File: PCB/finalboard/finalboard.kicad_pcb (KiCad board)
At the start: 2 copper layers, 132.1 x 76.2 mm, 1 part, among them U1 ESP32-S3-WROOM-1

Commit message: FinalBoard Changes
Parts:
- added U3: USBLC6-2SC6, Package_TO_SOT_SMD:SOT-23-6, F.Cu at (95.4, 93.0)
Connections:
- U1 pad 13: unconnected-(U1-GPIO19/U1RTS/ADC2_CH8/CLK_OUT2/USB_D--Pad13) -> /USB_D-
- U1 pad 14: unconnected-(U1-GPIO20/U1CTS/ADC2_CH9/CLK_OUT1/USB_D+-Pad14) -> /USB_D+
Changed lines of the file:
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@@
   (net 11 "unconnected-(U1-GPIO18{slash}U1RXD{slash}ADC2_CH7{slash}CLK_OUT3-Pad11)")
   (net 12 "unconnected-(U1-GPIO8{slash}TOUCH8{slash}ADC1_CH7{slash}SUBSPICS1-Pad12)")
-  (net 13 "unconnected-(U1-GPIO19{slash}U1RTS{slash}ADC2_CH8{slash}CLK_OUT2{slash}USB_D--Pad13)")
-  (net 14 "unconnected-(U1-GPIO20{slash}U1CTS{slash}ADC2_CH9{slash}CLK_OUT1{slash}USB_D+-Pad14)")
+  (net 13 "/USB_D-")
+  (net 14 "/USB_D+")
   (net 15 "unconnected-(U1-GPIO3{slash}TOUCH3{slash}ADC1_CH2-Pad15)")
   (net 16 "unconnected-(U1-GPIO46-Pad16)")
@@
   (net 38 "unconnected-(U1-GPIO2{slash}TOUCH2{slash}ADC1_CH1-Pad38)")
   (net 39 "unconnected-(U1-GPIO1{slash}TOUCH1{slash}ADC1_CH0-Pad39)")
+  (net 40 "/D+")
+  (net 41 "GND")
+  (net 42 "/D-")
+  (net 43 "Net-(J1-D--PadA7)")
+  (net 44 "Net-(U3-VBUS)")
+  (net 45 "Net-(J1-D+-PadA6)")
   (footprint "wc_sys_footprint:ESP32-S3-WROOM-1U" (layer "F.Cu")
     (at 95.39 60.33)
@@
       (net 12 "unconnected-(U1-GPIO8{slash}TOUCH8{slash}ADC1_CH7{slash}SUBSPICS1-Pad12)") (pinfunction "GPIO8/TOUCH8/ADC1_CH7/SUBSPICS1") (pintype "bidirectional"))
     (pad "13" smd rect (at -8.75 6.98) (size 1.5 0.9) (layers "F.Cu" "F.Paste" "F.Mask")
-      (net 13 "unconnected-(U1-GPIO19{slash}U1RTS{slash}ADC2_CH8{slash}CLK_OUT2{slash}USB_D--Pad13)") (pinfunction "GPIO19/U1RTS/ADC2_CH8/CLK_OUT2/USB_D-") (pintype "bidirectional"))
+      (net 13 "/USB_D-") (pinfunction "GPIO19/U1RTS/ADC2_CH8/CLK_OUT2/USB_D-") (pintype "bidirectional"))
     (pad "14" smd rect (at -8.75 8.25) (size 1.5 0.9) (layers "F.Cu" "F.Paste" "F.Mask")
-      (net 14 "unconnected-(U1-GPIO20{slash}U1CTS{slash}ADC2_CH9{slash}CLK_OUT1{slash}USB_D+-Pad14)") (pinfunction "GPIO20/U1CTS/ADC2_CH9/CLK_OUT1/USB_D+") (pintype "bidirectional"))
+      (net 14 "/USB_D+") (pinfunction "GPIO20/U1CTS/ADC2_CH9/CLK_OUT1/USB_D+") (pintype "bidirectional"))
     (pad "15" smd rect (at -6.985 9.5 90) (size 1.5 0.9) (layers "F.Cu" "F.Paste" "F.Mask")
       (net 15 "unconnected-(U1-GPIO3{slash}TOUCH3{slash}ADC1_CH2-Pad15)") (pinfunction "GPIO3/TOUCH3/ADC1_CH2") (pintype "bidirectional"))
@@
       (scale (xyz 1 1 1))
       (rotate (xyz 0 0 0))
+    )
+  )
+  (footprint "Package_TO_SOT_SMD:SOT-23-6" (layer "F.Cu")
+    (at 95.3825 93.03)
+    (descr "SOT, 6 Pin (https://www.jedec.org/sites/default/files/docs/Mo-178c.PDF variant AB), generated with kicad-footprint-generator ipc_gullwing_generator.py")
+    (tags "SOT TO_SOT_SMD")
+    (property "Sheetfile" "finalboard.kicad_sch")
+    (property "Sheetname" "")
+    (property "ki_description" "Very low capacitance ESD protection diode, 2 data-line, SOT-23-6")
+    (property "ki_keywords" "usb ethernet video")
+    (attr smd)
+    (fp_text reference "U3" (at 0 -2.4) (layer "F.SilkS")
+        (effects (font (size 1 1) (thickness 0.15)))
+    )
+    (fp_text value "USBLC6-2SC6" (at 0 2.4) (layer "F.Fab")
+        (effects (font (size 1 1) (thickness 0.15)))
+    )
+    (fp_text user "${REFERENCE}" (at 0 0) (layer "F.Fab")
+        (effects (font (size 0.4 0.4) (thickness 0.06)))
+    )
+    (fp_line (start 0 -1.56) (end -1.8 -1.56)
+      (stroke (width 0.12) (type solid)) (layer "F.SilkS"))
+    (fp_line (start 0 -1.56) (end 0.8 -1.56)
+      (stroke (width 0.12) (type solid)) (layer "F.SilkS"))
+    (fp_line (start 0 1.56) (end -0.8 1.56)
+      (stroke (width 0.12) (type solid)) (layer "F.SilkS"))
+    (fp_line (start 0 1.56) (end 0.8 1.56)
+      (stroke (width 0.12) (type solid)) (layer "F.SilkS"))
+    (fp_line (start -2.05 -1.7) (end -2.05 1.7)
+      (stroke (width 0.05) (type solid)) (layer "F.CrtYd"))
+    (fp_line (start -2.05 1.7) (end 2.05 1.7)
+      (stroke (width 0.05) (type solid)) (layer "F.CrtYd"))
+    (fp_line (start 2.05 -1.7) (end -2.05 -1.7)
+      (stroke (width 0.05) (type solid)) (layer "F.CrtYd"))
+    (fp_line (start 2.05 1.7) (end 2.05 -1.7)
+      (stroke (width 0.05) (type solid)) (layer "F.CrtYd"))
+    (fp_line (start -0.8 -1.05) (end -0.4 -1.45)
+      (stroke (width 0.1) (type solid)) (layer "F.Fab"))
+    (fp_line (start -0.8 1.45) (end -0.8 -1.05)
+      (stroke (width 0.1) (type solid)) (layer "F.Fab"))
+    (fp_line (start -0.4 -1.45) (end 0.8 -1.45)
+      (stroke (width 0.1) (type solid)) (layer "F.Fab"))
+    (fp_line (start 0.8 -1.45) (end 0.8 1.45)
+      (stroke (width 0.1) (type solid)) (layer "F.Fab"))
+    (fp_line (start 0.8 1.45) (end -0.8 1.45)
+      (stroke (width 0.1) (type solid)) (layer "F.Fab"))
+    (pad "1" smd roundrect (at -1.1375 -0.95) (size 1.325 0.6) (layers "F.Cu" "F.Paste" "F.Mask") (roundrect_rratio 0.25)
+      (net 40 "/D+") (pinfunction "I/O1") (pintype "passive"))
+    (pad "2" smd roundrect (at -1.1375 0) (size 1.325 0.6) (layers "F.Cu" "F.Paste" "F.Mask") (roundrect_rratio 0.25)
+      (net 41 "GND") (pinfunction "GND") (pintype "passive"))
+    (pad "3" smd roundrect (at -1.1375 0.95) (size 1.325 0.6) (layers "F.Cu" "F.Paste" "F.Mask") (roundrect_rratio 0.25)
+      (net 42 "/D-") (pinfunction "I/O2") (pintype "passive"))
+    (pad "4" smd roundrect (at 1.1375 0.95) (size 1.325 0.6) (layers "F.Cu" "F.Paste" "F.Mask") (roundrect_rratio 0.25)
+      (net 43 "Net-(J1-D--PadA7)") (pinfunction "I/O2") (pintype "passive"))
+    (pad "5" smd roundrect (at 1.1375 0) (size 1.325 0.6) (layers "F.Cu" "F.Paste" "F.Mask") (roundrect_rratio 0.25)
+      (net 44 "Net-(U3-VBUS)") (pinfunction "VBUS") (pintype "passive"))
+    (pad "6" smd roundrect (at 1.1375 -0.95) (size 1.325 0.6) (layers "F.Cu" "F.Paste" "F.Mask") (roundrect_rratio 0.25)
+      (net 45 "Net-(J1-D+-PadA6)") (pinfunction "I/O1") (pintype "passive"))
+    (model "${KICAD6_3DMODEL_DIR}/Package_TO_SOT_SMD.3dshapes/SOT-23-6.wrl"
+      (offset (xyz 0 0 0))
+      (scale (xyz 1 1 1))
+      (rotate (xyz 0 0 0))

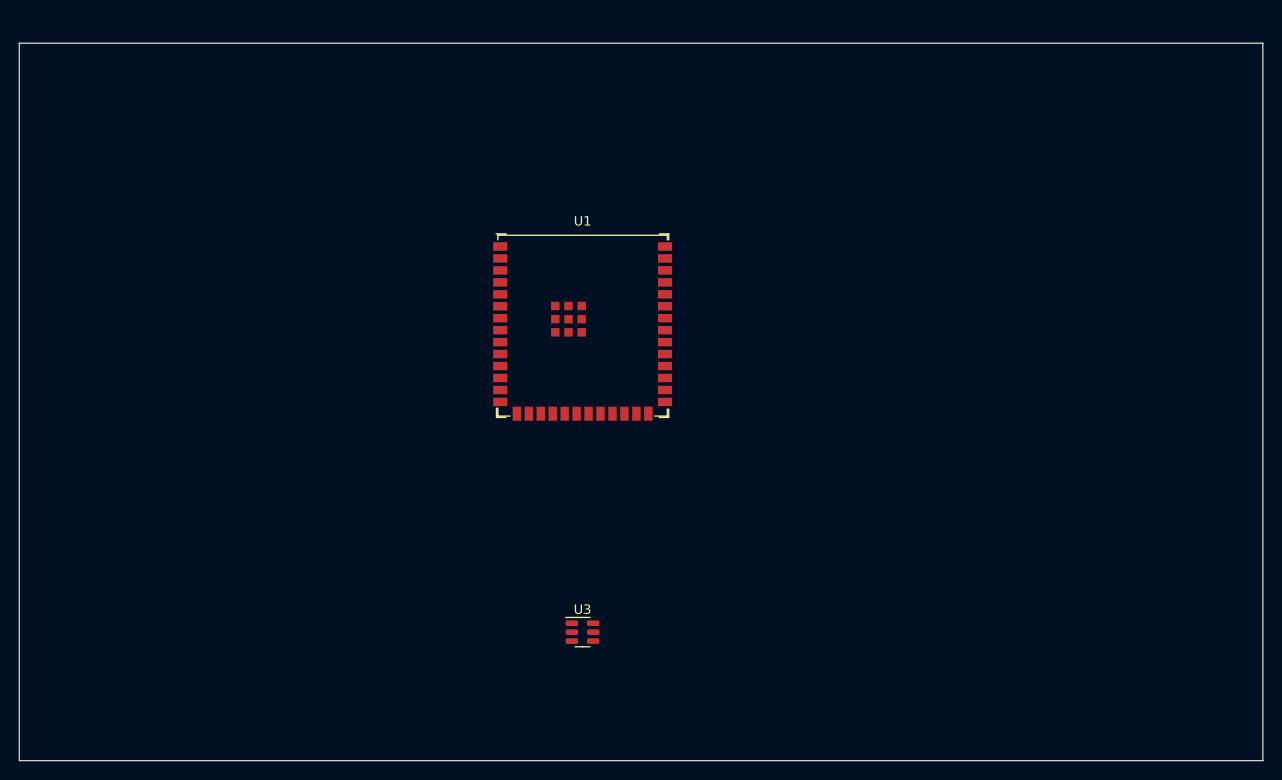
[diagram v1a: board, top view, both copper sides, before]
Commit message: Design Iterations
added touch buttons
wired SPI sdcard and display
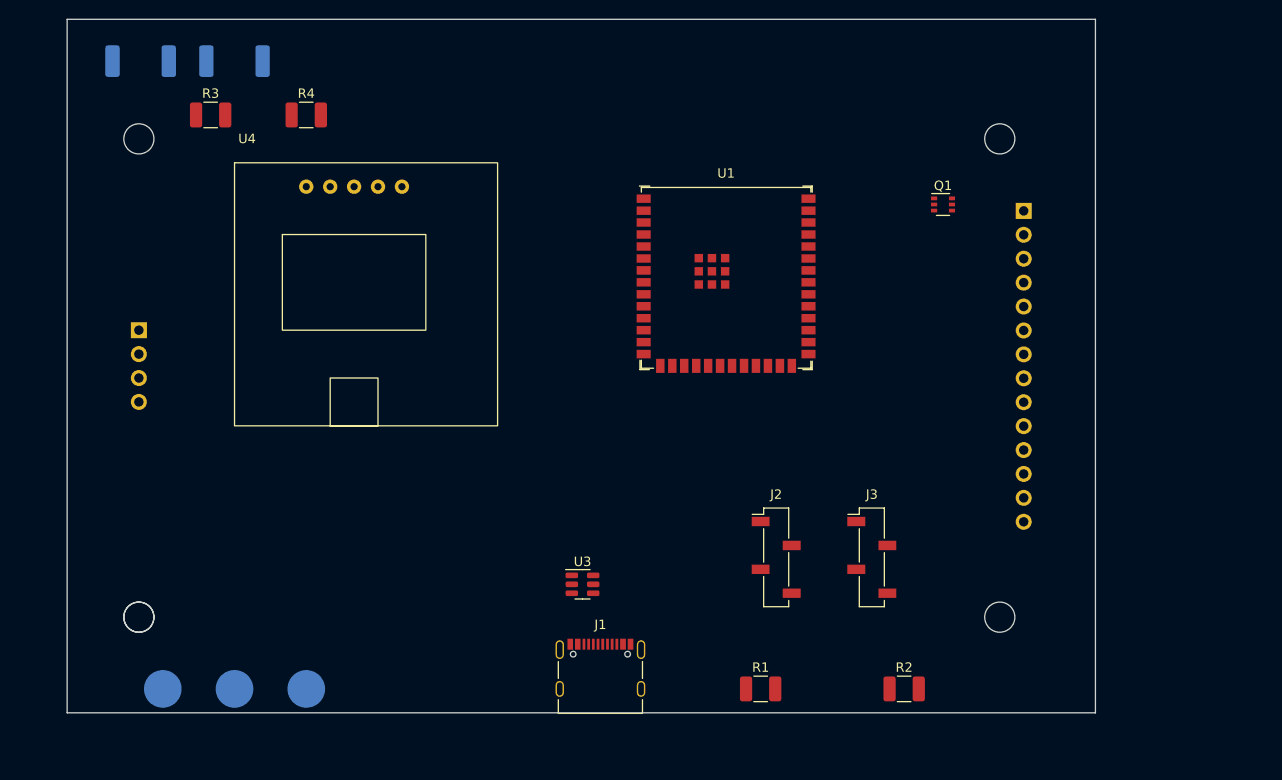
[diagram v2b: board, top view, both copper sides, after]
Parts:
- added ?: , , F.Cu at (48.3, 91.4)
- added D1: LED, LED_SMD:LED_2512_6332Metric_Pad1.52x3.35mm_HandSolder, B.Cu at (48.4, 32.4)
- added D2: LED, LED_SMD:LED_2512_6332Metric_Pad1.52x3.35mm_HandSolder, B.Cu at (58.4, 32.4)
- added G***: LOGO, wc_sys_footprint:medlogo, B.Cu at (139.7, 31.7)
- added J1: USB_C_Receptacle_USB2.0, Connector_USB:USB_C_Receptacle_Palconn_UTC16-G, F.Cu at (97.3, 96.8)
- added J2: Conn_01x04, Connector_PinSocket_2.54mm:PinSocket_1x04_P2.54mm_Vertical_SMD_Pin1Left, F.Cu at (116.0, 85.1)
- added J3: Conn_01x04, Connector_PinSocket_2.54mm:PinSocket_1x04_P2.54mm_Vertical_SMD_Pin1Left, F.Cu at (126.1, 85.1)
- added Q1: MMDT3904, Package_TO_SOT_SMD:SOT-363_SC-70-6, F.Cu at (133.7, 47.6)
- added R1: 5k, Resistor_SMD:R_1210_3225Metric_Pad1.30x2.65mm_HandSolder, F.Cu at (114.3, 99.1)
- added R2: 5k, Resistor_SMD:R_1210_3225Metric_Pad1.30x2.65mm_HandSolder, F.Cu at (129.5, 99.1)
- added R3: R, Resistor_SMD:R_1210_3225Metric_Pad1.30x2.65mm_HandSolder, F.Cu at (55.9, 38.1)
- added R4: R, Resistor_SMD:R_1210_3225Metric_Pad1.30x2.65mm_HandSolder, F.Cu at (66.0, 38.1)
- added REF**: MountingHole_3.2mm_M3, MountingHole:MountingHole_3.2mm_M3, F.Cu at (139.7, 91.4)
- added REF**: MountingHole_3.2mm_M3, MountingHole:MountingHole_3.2mm_M3, F.Cu at (48.3, 40.6)
- added REF**: MountingHole_3.2mm_M3, MountingHole:MountingHole_3.2mm_M3, F.Cu at (139.7, 40.6)
- added REF**: MountingHole_3.2mm_M3, MountingHole:MountingHole_3.2mm_M3, F.Cu at (48.3, 91.4)
- added TP1: TestPoint, TestPoint:TestPoint_Pad_D4.0mm, B.Cu at (66.0, 99.1)
- added TP2: TestPoint, TestPoint:TestPoint_Pad_D4.0mm, B.Cu at (58.4, 99.1)
- added TP3: TestPoint, TestPoint:TestPoint_Pad_D4.0mm, B.Cu at (50.8, 99.1)
- added U2: ~, wc_sys_footprint:LCD3.5tft, B.Cu at (93.3, 65.4)
- added U4: ~, wc_sys_footprint:NEO-6M, F.Cu at (71.1, 55.9)
- moved U1 16.1 mm to (110.6, 55.2)
- moved U3 5.08 mm to (95.4, 88.0)
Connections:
- U1 pad 1: Net-(U1-GND-Pad1) -> GND
- U1 pad 10: unconnected-(U1-GPIO17/U1TXD/ADC2_CH6-Pad10) -> /ESP_RX1
- U1 pad 11: unconnected-(U1-GPIO18/U1RXD/ADC2_CH7/CLK_OUT3-Pad11) -> /ESP_TX2
- U1 pad 12: unconnected-(U1-GPIO8/TOUCH8/ADC1_CH7/SUBSPICS1-Pad12) -> Net-(D1-A)
- U1 pad 15: unconnected-(U1-GPIO3/TOUCH3/ADC1_CH2-Pad15) -> Net-(U1-GPIO3/TOUCH3/ADC1_CH2)
- U1 pad 17: unconnected-(U1-GPIO9/TOUCH9/ADC1_CH8/FSPIHD/SUBSPIHD-Pad17) -> Net-(D2-A)
- U1 pad 18: unconnected-(U1-GPIO10/TOUCH10/ADC1_CH9/FSPICS0/FSPIIO4/SUBSPICS0-Pad18) -> /SS1
- U1 pad 19: unconnected-(U1-GPIO11/TOUCH11/ADC2_CH0/FSPID/FSPIIO5/SUBSPID-Pad19) -> /MOSI
- U1 pad 2: unconnected-(U1-3V3-Pad2) -> +3V3
- U1 pad 20: unconnected-(U1-GPIO12/TOUCH12/ADC2_CH1/FSPICLK/FSPIIO6/SUBSPICLK-Pad20) -> /SCK
- U1 pad 21: unconnected-(U1-GPIO13/TOUCH13/ADC2_CH2/FSPIQ/FSPIIO7/SUBSPIQ-Pad21) -> /MISO
- U1 pad 22: unconnected-(U1-GPIO14/TOUCH14/ADC2_CH3/FSPIWP/FSPIDQS/SUBSPIWP-Pad22) -> /ESP_TX1
- U1 pad 23: unconnected-(U1-GPIO21-Pad23) -> /ESP_RX2
- U1 pad 36: unconnected-(U1-U0RXD/GPIO44/CLK_OUT2-Pad36) -> /ESP_RX0
- U1 pad 37: unconnected-(U1-U0TXD/GPIO43/CLK_OUT1-Pad37) -> /ESP_TX0
- U1 pad 38: unconnected-(U1-GPIO2/TOUCH2/ADC1_CH1-Pad38) -> /PWR_TRAN_TFT
- U1 pad 39: unconnected-(U1-GPIO1/TOUCH1/ADC1_CH0-Pad39) -> /PWR_TRAN_LCD
- U1 pad 4: unconnected-(U1-GPIO4/TOUCH4/ADC1_CH3-Pad4) -> Net-(U1-GPIO4/TOUCH4/ADC1_CH3)
- U1 pad 40: Net-(U1-GND-Pad1) -> GND
- U1 pad 41: Net-(U1-GND-Pad1) -> GND
- U1 pad 5: unconnected-(U1-GPIO5/TOUCH5/ADC1_CH4-Pad5) -> Net-(U1-GPIO5/TOUCH5/ADC1_CH4)
- U1 pad 6: unconnected-(U1-GPIO6/TOUCH6/ADC1_CH5-Pad6) -> /ESP_SS_TX0
- U1 pad 7: unconnected-(U1-GPIO7/TOUCH7/ADC1_CH6-Pad7) -> /ESP_SS_RX0
- U3 pad 1: /D+ -> /USB_D+
- U3 pad 3: /D- -> /USB_D-
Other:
- board size 132.1 x 76.2 mm -> 109.2 x 73.7 mm
- board text added: "Electrathon Communication System"
- board text added: "Recording"
- board text added: "WiFi ON"
- board text added: "↓ Insert SD Card ↓"

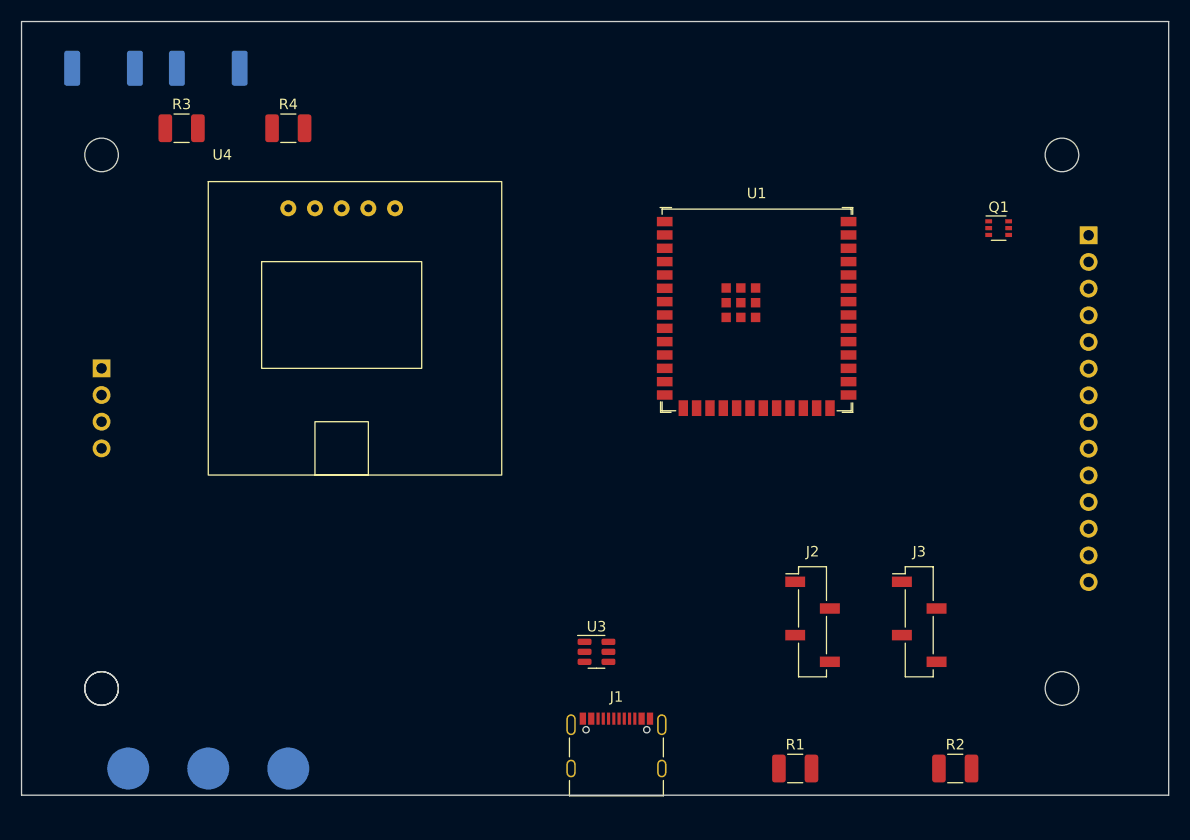
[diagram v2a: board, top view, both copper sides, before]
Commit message: Added Components
added lipo charger, regulator, removed type B usb, added 3d Models
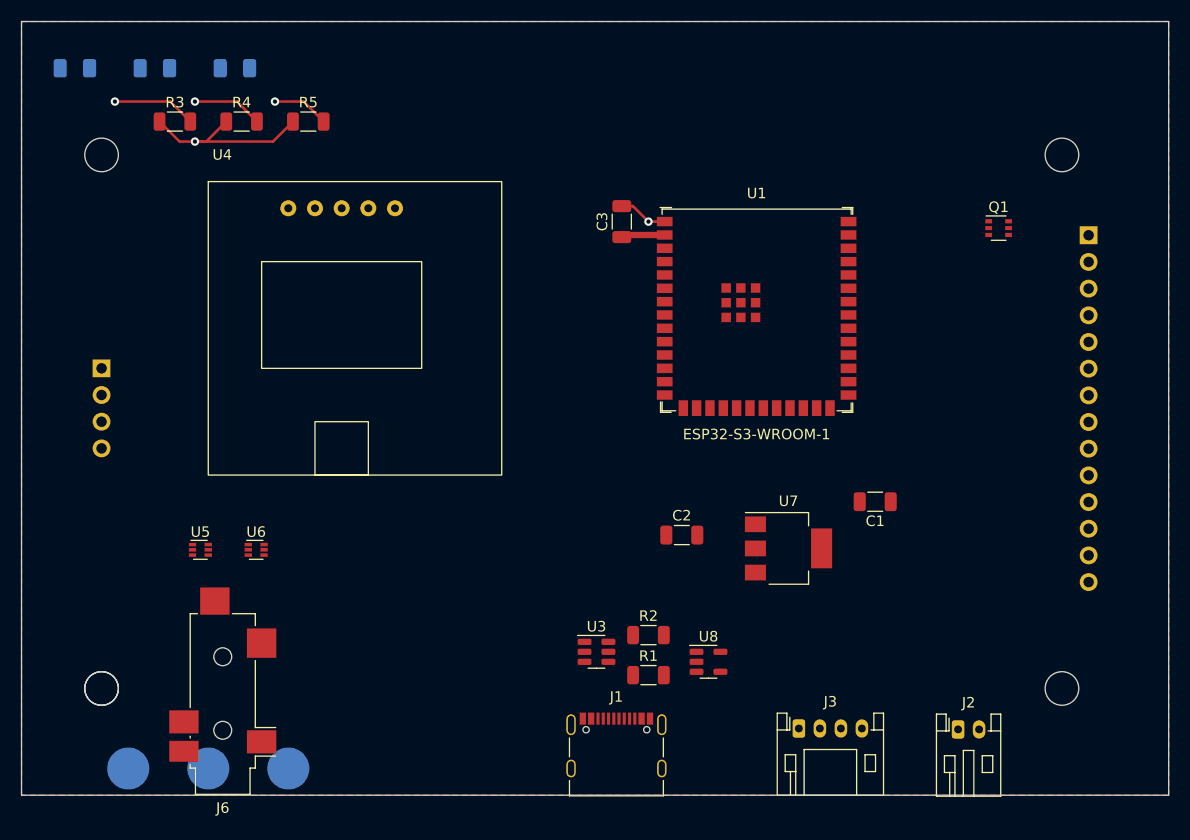
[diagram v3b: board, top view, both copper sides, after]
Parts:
- added C1: 10u, Capacitor_SMD:C_1206_3216Metric, F.Cu at (121.9, 73.7)
- added C2: 10u, Capacitor_SMD:C_1206_3216Metric, F.Cu at (103.5, 76.8)
- added C3: 10u, Capacitor_SMD:C_1206_3216Metric, F.Cu at (97.8, 47.0)
- added D3: LED, LED_SMD:LED_1206_3216Metric, B.Cu at (61.0, 32.4)
- added J6: AudioJack4, Connector_Audio:Jack_3.5mm_CUI_SJ2-3593D-SMT_Horizontal, F.Cu at (59.8, 92.9)
- added R5: R, Resistor_SMD:R_1206_3216Metric, F.Cu at (67.9, 37.5)
- added U5: SN74LVC1T45DRL, Package_TO_SOT_SMD:SOT-563, F.Cu at (57.7, 78.2)
- added U6: SN74LVC1T45DRL, Package_TO_SOT_SMD:SOT-563, F.Cu at (63.0, 78.2)
- added U7: AMS1117-3.3, Package_TO_SOT_SMD:SOT-223-3_TabPin2, F.Cu at (113.7, 78.1)
- added U8: MCP73831-2-OT, Package_TO_SOT_SMD:SOT-23-5, F.Cu at (106.0, 88.9)
- D1, D2: footprint LED_SMD:LED_2512_6332Metric_Pad1.52x3.35mm_HandSolder -> LED_SMD:LED_1206_3216Metric
- J2: value Conn_01x04 -> Conn_01x02; footprint Connector_PinSocket_2.54mm:PinSocket_1x04_P2.54mm_Vertical_SMD_Pin1Left -> Connector_JST:JST_PH_S2B-PH-K_1x02_P2.00mm_Horizontal
- J3: footprint Connector_PinSocket_2.54mm:PinSocket_1x04_P2.54mm_Vertical_SMD_Pin1Left -> Connector_JST:JST_PH_S4B-PH-K_1x04_P2.00mm_Horizontal
- R1, R2, R3, R4: footprint Resistor_SMD:R_1210_3225Metric_Pad1.30x2.65mm_HandSolder -> Resistor_SMD:R_1206_3216Metric
- moved R2 31.9 mm to (100.3, 86.4)
- moved J2 17.2 mm to (129.8, 95.3)
- moved R1 16.6 mm to (100.3, 90.2)
- moved J3 15.3 mm to (114.7, 95.2)
- moved D2 5.08 mm to (53.3, 32.4)
- moved R4 4.49 mm to (61.6, 37.5)
- moved D1 2.73 mm to (45.7, 32.4)
- moved R3 0.90 mm to (55.2, 37.5)
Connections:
- J2 pad 2: /ESP_TX1 -> unconnected-(J2-Pin_2-Pad2)
- U1 pad 31: unconnected-(U1-GPIO38/FSPIWP/SUBSPIWP-Pad31) -> Net-(D3-A)
- U4 pad 1: Net-(U3-VBUS) -> +3V3
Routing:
- net GND: track 0.00 -> 22.8 mm, vias 0 -> 2
- net Net-(D1-K): track 0.00 -> 7.97 mm, vias 0 -> 1
- net Net-(D2-K): track 0.00 -> 6.70 mm, vias 0 -> 1
- net Net-(D3-K): track 0.00 -> 5.43 mm, vias 0 -> 1
- net +3V3: track 0.00 -> 4.17 mm
- added copper zone on F.Cu, net +3V3
- added copper zone on In1.Cu, net GND
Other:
- copper layers 2 -> 4
- board text added: "SDCard"
